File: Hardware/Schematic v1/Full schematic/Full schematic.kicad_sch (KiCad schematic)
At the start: 324 parts, among them J1 Conn_01x02_Male, J10 Conn_01x01_Male, J2 Reset, J3 Encoder, J4 Failure LED, J5 Bluetooth, J6 Conn_01x02_Male, J7 Display, J8 Buttons, J9 Conn_01x02_Male, K1 EDR101A0500, K2 EDR101A0500, K3 EDR101A0500, K4 EDR101A0500, K5 EDR101A0500, K6 EDR101A0500, Q1 BC847, Q10 IRLML6402, Q11 BC847, Q12 IRFZ44, Q13 BC847, Q14 BSS138, Q15 BC847, Q16 IRF610, Q17 BC847, Q18 IRLML6402, Q19 BC847, Q2 BC847, Q20 BFS17, Q21 IRLML6402, Q22 AFT05MS003N, Q23 IRLML2502, Q24 IRLML2502, Q25 IRLML2502, Q26 IRLML2502, Q27 IRLML2502, Q28 IRLML2502, Q3 BC847, Q4 BC847, Q5 BC847, Q6 IRLML6402, Q7 IRF4905, Q8 IRLML6402, Q9 IRLML6402, U1 74LVC2T45DC, U10 ICS501, U11 STM32F103C8Tx, U12 CAT24C256, U2 74LVC2T45DC, U3 AD9835, U4 LM27313XMF, U5 LM2734X, U6 LM2734X, U7 MAX1837EUT33-T, U8 UC3843_SOIC8, U9 AD5245BRJZ10, X1 50MHz, Y1 8MHz, Y2 32768Hz

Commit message: MCU is able to shut-down most of 3.3V-powered circuits to reduce battery consumption
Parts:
- added Q?: BC847, Package_TO_SOT_SMD:SOT-23, symbol Transistor_BJT:BC847
- added Q?: IRLML6402, Package_TO_SOT_SMD:SOT-23, symbol Transistor_FET:IRLML6402
- added R? (x2): 10k, Resistor_SMD:R_0805_2012Metric_Pad1.20x1.40mm_HandSolder, symbol Device:R
- added R?: 10, Resistor_SMD:R_0805_2012Metric_Pad1.20x1.40mm_HandSolder, symbol Device:R
- added R?: 47k, Resistor_SMD:R_0805_2012Metric_Pad1.20x1.40mm_HandSolder, symbol Device:R
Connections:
- net GND: now also Q?.2 (E), R?.2
- net REG_3.3V: now also Q?.2 (S), R?.1; no longer C106.2, C2.1, C3.1, C62.1, R76.1, R78.1, R82.1, R84.1, R85.1, R86.1, R88.1, R89.1, R90.1, U1.1 (VCCA), U1.5 (DIR), U12.8 (VCC), U2.1 (VCCA), U2.5 (DIR), U9.2 (Vdd)
- net ACTIVATE_3.3V: now reaches U11.28 (PB15)
- net ACTIVATE_3.3V: now also R?.1, R?.2
- new net: Q?.1 (B), R?.1
- new net: Q?.3 (C), R?.2
- new net: Q?.1 (G), R?.1, R?.2
- new net SW_3.3V: C106.2, C2.1, C3.1, C62.1, Q?.3 (D), R76.1, R78.1, R82.1, R84.1, R85.1, R86.1, R88.1, R89.1, R90.1, U1.1 (VCCA), U1.5 (DIR), U12.8 (VCC), U2.1 (VCCA), U2.5 (DIR), U9.2 (Vdd)
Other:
- note added: "Switcheable 3.3V"
- moved on the sheet: R11, R17, R4, R5

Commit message: Removed 30 capacitors from antenna tuner by swithcing to high-voltage capacitors
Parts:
- removed C100, C101, C102, C103, C104: 200pF, Capacitor_SMD:C_0805_2012Metric_Pad1.18x1.45mm_HandSolder, symbol Device:C
- removed C112, C113, C114, C115, C116: 100pF, Capacitor_SMD:C_0805_2012Metric_Pad1.18x1.45mm_HandSolder, symbol Device:C
- removed C118, C119, C120, C121, C122: 47pF, Capacitor_SMD:C_0805_2012Metric_Pad1.18x1.45mm_HandSolder, symbol Device:C
- removed C124, C125, C126, C127, C128: 24pF, Capacitor_SMD:C_0805_2012Metric_Pad1.18x1.45mm_HandSolder, symbol Device:C
- removed C130, C131, C132, C133, C134: 12pF, Capacitor_SMD:C_0805_2012Metric_Pad1.18x1.45mm_HandSolder, symbol Device:C
- removed C85, C86, C87, C88, C89: 390pF, Capacitor_SMD:C_0805_2012Metric_Pad1.18x1.45mm_HandSolder, symbol Device:C
- added C?: 2pF 250V, Capacitor_SMD:C_0805_2012Metric_Pad1.18x1.45mm_HandSolder, symbol Device:C
- C105: value 200pF -> 32pF 250V
- C117: value 100pF -> 16pF 250V
- C123: value 47pF -> 8pF 250V
- C129: value 24pF -> 4pF 250V
- C135: value 12pF -> 2pF 250V
- C90: value 390pF -> 62pF 250V
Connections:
- net ANT_3.5: now also C105.1, C117.1, C123.1, C129.1, C135.1, C90.1, C?.1
- net at C90.2, K1.1: now also C?.2
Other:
- note removed: "16pF"
- note removed: "2pF"
- note removed: "32pF"
- note removed: "4pF"
- note removed: "64pF"
- note removed: "8pF"
- moved on the sheet: C1, C10, C105, C106, C107, C108, C109, C11, C110, C111, C117, C12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

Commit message: New antenna matcher with smaller relays
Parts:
- removed C105: 32pF 250V, Capacitor_SMD:C_0805_2012Metric_Pad1.18x1.45mm_HandSolder, symbol Device:C
- removed C117: 16pF 250V, Capacitor_SMD:C_0805_2012Metric_Pad1.18x1.45mm_HandSolder, symbol Device:C
- removed C123: 8pF 250V, Capacitor_SMD:C_0805_2012Metric_Pad1.18x1.45mm_HandSolder, symbol Device:C
- removed C129: 4pF 250V, Capacitor_SMD:C_0805_2012Metric_Pad1.18x1.45mm_HandSolder, symbol Device:C
- removed K1, K2, K3, K4, K5, K6: EDR101A0500, Relay_THT:Relay_SPST_StandexMeder_SIL_Form1A, symbol Full-schematic-rescue:EDR101A0500-Fossa_library
- removed Q23, Q24: IRLML2502, Package_TO_SOT_SMD:SOT-23, symbol Device:Q_NMOS_GSD
- removed R87, R92, R93, R94: 100, Resistor_SMD:R_0805_2012Metric_Pad1.20x1.40mm_HandSolder, symbol Device:R
- added C101: 16pF 250V, Capacitor_SMD:C_0805_2012Metric_Pad1.18x1.45mm_HandSolder, symbol Device:C
- added C102: 8pF 250V, Capacitor_SMD:C_0805_2012Metric_Pad1.18x1.45mm_HandSolder, symbol Device:C
- added C103: 4pF 250V, Capacitor_SMD:C_0805_2012Metric_Pad1.18x1.45mm_HandSolder, symbol Device:C
- added C94: 32pF 250V, Capacitor_SMD:C_0805_2012Metric_Pad1.18x1.45mm_HandSolder, symbol Device:C
- added K1, K2, K3, K4, K5, K6: G6L-1F-DC5, G6L-1F-DC5, symbol G6L-1F-DC5:G6L-1F-DC5
- added Q28, Q29: IRLML2502, Package_TO_SOT_SMD:SOT-23, symbol Device:Q_NMOS_GSD
- added R95, R96, R97, R98: 100, Resistor_SMD:R_0805_2012Metric_Pad1.20x1.40mm_HandSolder, symbol Device:R
- gave numbers to parts that had none: 7
- renumbered C111 to C100, C135 to C104, C110 to C105, C109 to C106, C24 to C23, C23 to C24, C30 to C29, C29 to C30, C43 to C41, C41 to C42, C42 to C43, C57 to C56, C56 to C57, C69 to C68, C68 to C69, C84 to C85, C90 to C86, C91 to C87, C92 to C88, C93 to C89, C94 to C90, C95 to C91, C96 to C92, C97 to C93, C99 to C95, C98 to C96, C106 to C97, C108 to C98, C107 to C99, Q13 to Q15, Q14 to Q16, Q15 to Q17, Q16 to Q18, Q17 to Q19, Q18 to Q20, Q19 to Q21, Q21 to Q22, Q20 to Q23, Q22 to Q24, Q28 to Q30, R23 to R24, R24 to R25, R25 to R26, R26 to R27, R27 to R28, R28 to R29, R31 to R30, R29 to R31, R30 to R32, R32 to R34, R34 to R35, R35 to R36, R36 to R37, R37 to R38, R38 to R39, R39 to R40, R40 to R41, R41 to R42, R42 to R43, R43 to R44, R44 to R45, R45 to R46, R46 to R47, R47 to R48, R48 to R52, R49 to R53, R50 to R54, R51 to R55, R52 to R56, R53 to R57, R54 to R58, R55 to R59, R56 to R60, R57 to R61, R58 to R62, R59 to R63, R60 to R64, R61 to R65, R62 to R66, R63 to R67, R64 to R68, R65 to R69, R66 to R70, R68 to R71, R67 to R72, R69 to R73, R70 to R74, R71 to R75, R72 to R76, R73 to R77, R74 to R78, R75 to R79, R76 to R80, R77 to R81, R79 to R82, R78 to R83, R80 to R84, R81 to R85, R82 to R86, R83 to R87, R84 to R88, R85 to R89, R86 to R90, R88 to R92, R89 to R93, R90 to R94, R95 to R99
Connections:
- net ANT_3.5: now also C101.1, C102.1, C103.1, C94.1
- net GND: now also K1.2 (4), K2.2 (4), K3.2 (4), K4.2 (4), K5.2 (4), K6.2 (4), Q28.2 (S), Q29.2 (S)
- net MATCH_1: now also R98.2
- net MATCH_2: now also R97.2
- net MATCH_3: now also R96.2
- net MATCH_4: now also R95.2; no longer R91.2
- net MATCH_5: now also R91.2
- net PWR_3.5_5: now also K1.4 (8), K2.4 (8), K3.4 (8), K4.4 (8), K5.4 (8), K6.4 (8)
- net at C84.2, C86.2: now also K1.1 (2)
- net at Q25.3 (D): now also K1.3 (5)
- net at Q26.3 (D): now also K2.3 (5)
- net at Q27.3 (D): now also K3.3 (5)
- net at R91.1: now also Q25.1 (G)
- net at Q26.1 (G): now also R95.1
- net at Q27.1 (G): now also R96.1
- net at C104.2: now also K6.1 (2)
- net at Q30.3 (D): now also K6.3 (5)
- new net: Q29.1 (G), R98.1
- new net: K5.3 (5), Q29.3 (D)
- new net: C94.2, K2.1 (2)
- new net: C103.2, K5.1 (2)
- new net: C102.2, K4.1 (2)
- new net: K4.3 (5), Q28.3 (D)
- new net: C101.2, K3.1 (2)
- new net: Q28.1 (G), R97.1
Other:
- moved on the sheet: C104, C105, C106, C84, C86, Q30, R99

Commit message: Prepared to start PCB tracing
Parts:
- K1, K2, K3, K4, K5, K6: footprint G6L-1F-DC5 -> SamacSys:G6L-1F-DC5
- U7: footprint (none) -> Package_TO_SOT_SMD:TSOT-23-6
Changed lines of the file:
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@@
     (property "Reference" "U7" (id 0) (at 165.1 392.591 0))
     (property "Value" "MAX1837EUT33-T" (id 1) (at 165.1 395.1279 0))
-    (property "Footprint" " " (id 2) (at 165.1 394.97 0)
+    (property "Footprint" "Package_TO_SOT_SMD:TSOT-23-6" (id 2) (at 165.1 394.97 0)
       (effects (font (size 1.27 1.27)) hide)
     )
@@
     (property "Reference" "K2" (id 0) (at 459.105 38.261 0))
     (property "Value" "G6L-1F-DC5" (id 1) (at 459.105 40.7979 0))
-    (property "Footprint" "G6L-1F-DC5" (id 2) (at 465.455 41.91 0)
+    (property "Footprint" "SamacSys:G6L-1F-DC5" (id 2) (at 465.455 41.91 0)
       (effects (font (size 1.27 1.27)) (justify left) hide)
     )
@@
     (property "Reference" "K5" (id 0) (at 541.02 38.261 0))
     (property "Value" "G6L-1F-DC5" (id 1) (at 541.02 40.7979 0))
-    (property "Footprint" "G6L-1F-DC5" (id 2) (at 547.37 41.91 0)
+    (property "Footprint" "SamacSys:G6L-1F-DC5" (id 2) (at 547.37 41.91 0)
       (effects (font (size 1.27 1.27)) (justify left) hide)
     )
@@
     (property "Reference" "K4" (id 0) (at 513.715 38.261 0))
     (property "Value" "G6L-1F-DC5" (id 1) (at 513.715 40.7979 0))
-    (property "Footprint" "G6L-1F-DC5" (id 2) (at 520.065 41.91 0)
+    (property "Footprint" "SamacSys:G6L-1F-DC5" (id 2) (at 520.065 41.91 0)
       (effects (font (size 1.27 1.27)) (justify left) hide)
     )
@@
     (property "Reference" "K1" (id 0) (at 431.8 38.261 0))
     (property "Value" "G6L-1F-DC5" (id 1) (at 431.8 40.7979 0))
-    (property "Footprint" "G6L-1F-DC5" (id 2) (at 438.15 41.91 0)
+    (property "Footprint" "SamacSys:G6L-1F-DC5" (id 2) (at 438.15 41.91 0)
       (effects (font (size 1.27 1.27)) (justify left) hide)
     )
@@
     (property "Reference" "K6" (id 0) (at 568.325 38.261 0))
     (property "Value" "G6L-1F-DC5" (id 1) (at 568.325 40.7979 0))
-    (property "Footprint" "G6L-1F-DC5" (id 2) (at 574.675 41.91 0)
+    (property "Footprint" "SamacSys:G6L-1F-DC5" (id 2) (at 574.675 41.91 0)
       (effects (font (size 1.27 1.27)) (justify left) hide)
     )
@@
     (property "Reference" "K3" (id 0) (at 486.41 38.261 0))
     (property "Value" "G6L-1F-DC5" (id 1) (at 486.41 40.7979 0))
-    (property "Footprint" "G6L-1F-DC5" (id 2) (at 492.76 41.91 0)
+    (property "Footprint" "SamacSys:G6L-1F-DC5" (id 2) (at 492.76 41.91 0)
       (effects (font (size 1.27 1.27)) (justify left) hide)
     )
@@
     )
     (path "/a2e1440b-e257-4d0a-808d-5710ecf6f920"
-      (reference "K1") (unit 1) (value "G6L-1F-DC5") (footprint "G6L-1F-DC5")
+      (reference "K1") (unit 1) (value "G6L-1F-DC5") (footprint "SamacSys:G6L-1F-DC5")
     )
     (path "/324106b3-abb2-420f-a627-0aac5e60675f"
-      (reference "K2") (unit 1) (value "G6L-1F-DC5") (footprint "G6L-1F-DC5")
+      (reference "K2") (unit 1) (value "G6L-1F-DC5") (footprint "SamacSys:G6L-1F-DC5")
     )
     (path "/d89a0302-120b-4752-9963-58f61b530fff"
-      (reference "K3") (unit 1) (value "G6L-1F-DC5") (footprint "G6L-1F-DC5")
+      (reference "K3") (unit 1) (value "G6L-1F-DC5") (footprint "SamacSys:G6L-1F-DC5")
     )
     (path "/4aa9f57c-e3bb-4992-9327-b49e49f538a5"
-      (reference "K4") (unit 1) (value "G6L-1F-DC5") (footprint "G6L-1F-DC5")
+      (reference "K4") (unit 1) (value "G6L-1F-DC5") (footprint "SamacSys:G6L-1F-DC5")
     )
     (path "/423851f6-93ed-4dfc-9519-566e79596147"
-      (reference "K5") (unit 1) (value "G6L-1F-DC5") (footprint "G6L-1F-DC5")
+      (reference "K5") (unit 1) (value "G6L-1F-DC5") (footprint "SamacSys:G6L-1F-DC5")
     )
     (path "/bc52d2ea-23a3-403b-8c59-ec7d15d1e2a6"
-      (reference "K6") (unit 1) (value "G6L-1F-DC5") (footprint "G6L-1F-DC5")
+      (reference "K6") (unit 1) (value "G6L-1F-DC5") (footprint "SamacSys:G6L-1F-DC5")
     )
     (path "/00000000-0000-0000-0000-000060d7cf1a"
@@
     )
     (path "/2d6c91ba-d03a-44df-a397-8d992093a3d4"
-      (reference "U7") (unit 1) (value "MAX1837EUT33-T") (footprint " ")
+      (reference "U7") (unit 1) (value "MAX1837EUT33-T") (footprint "Package_TO_SOT_SMD:TSOT-23-6")
     )
     (path "/00000000-0000-0000-0000-000060b1e62b"

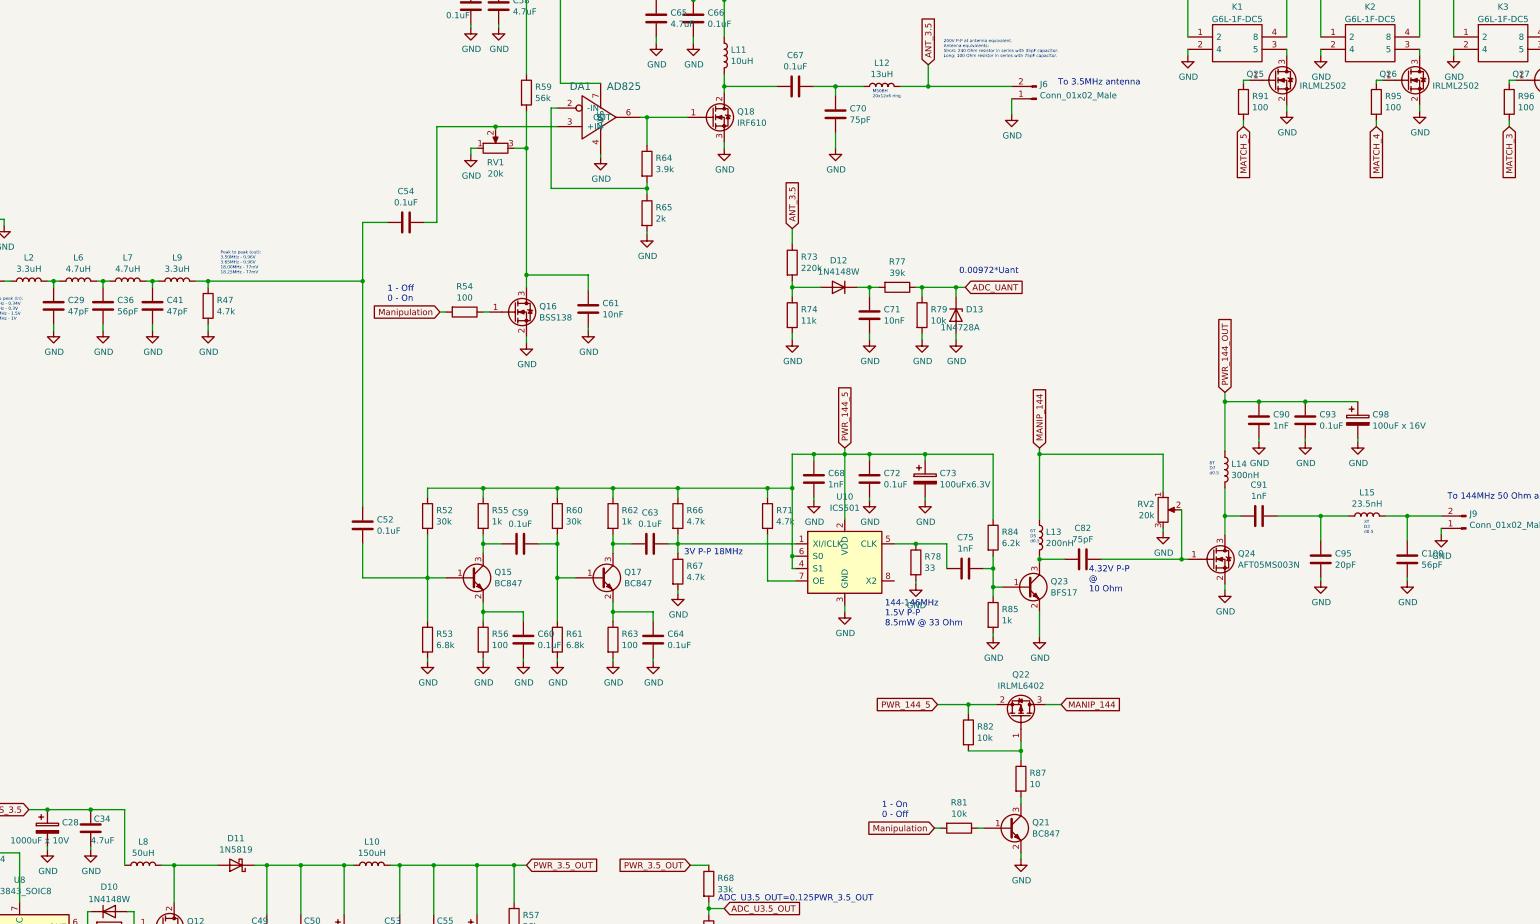
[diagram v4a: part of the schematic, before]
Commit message: All inductors are SMD now
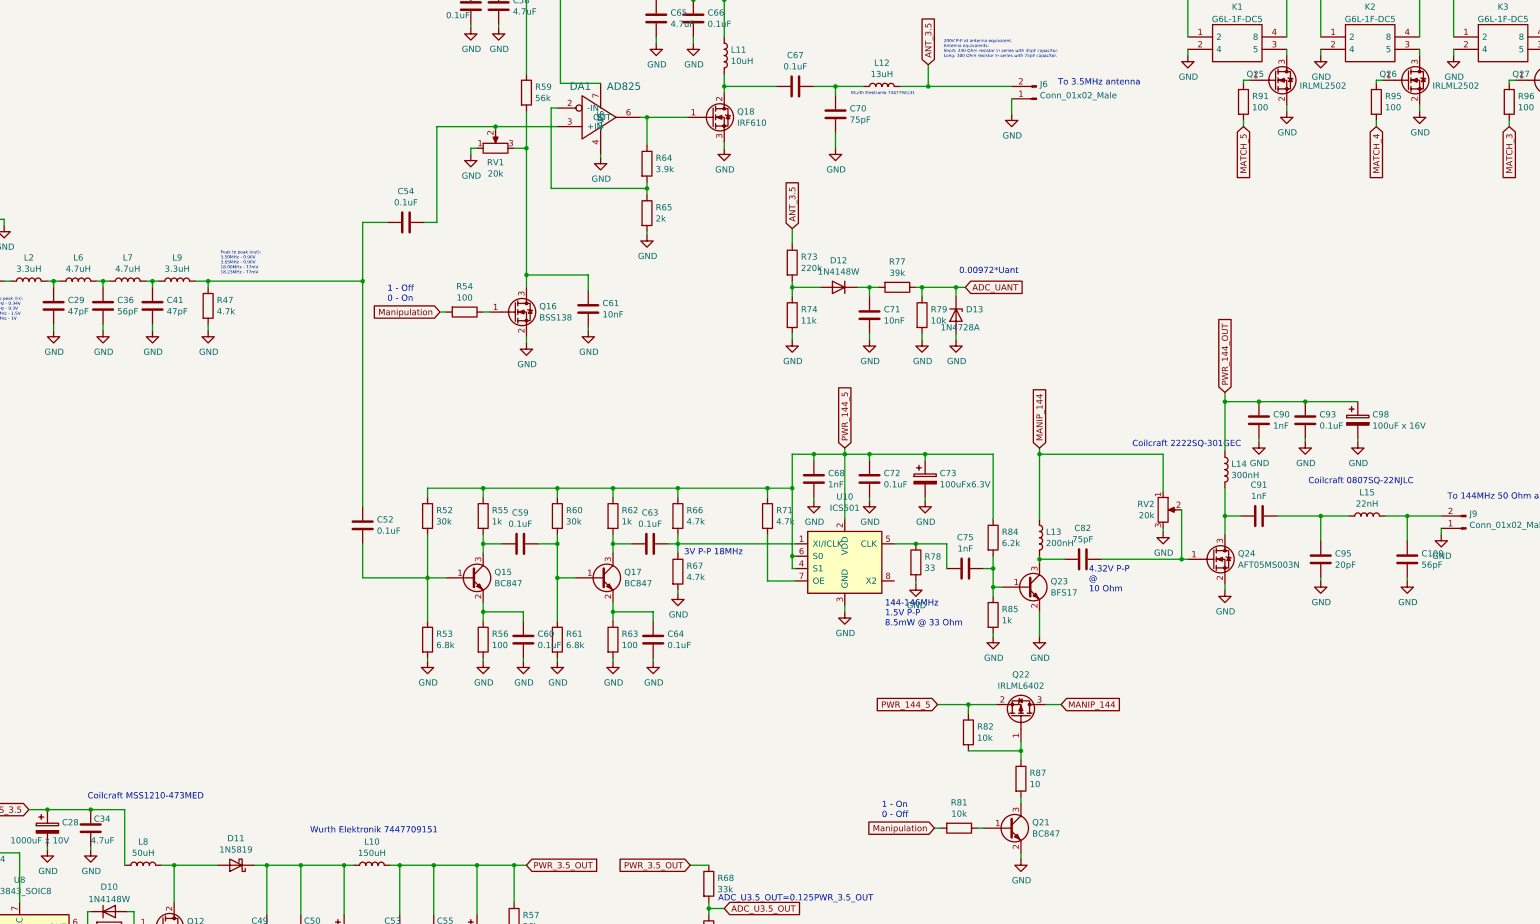
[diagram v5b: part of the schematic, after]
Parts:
- C1: footprint Capacitor_THT:CP_Radial_D6.3mm_P2.50mm -> Inductor_SMD:L_0603_1608Metric_Pad1.05x0.95mm_HandSolder
- L12: footprint Inductor_THT:L_Toroid_Vertical_L21.6mm_W9.1mm_P8.40mm_Bourns_5700 -> Inductor_SMD:L_10.4x10.4_H4.8
- L13: footprint Inductor_THT:L_Axial_L5.3mm_D2.2mm_P7.62mm_Horizontal_Vishay_IM-1 -> Inductor_SMD:L_0603_1608Metric_Pad1.05x0.95mm_HandSolder
- L14: footprint Inductor_THT:L_Axial_L16.0mm_D7.5mm_P7.62mm_Vertical_Fastron_XHBCC -> Inductor_SMD:L_Pulse_PA4320
- L15: value 23.5nH -> 22nH; footprint Inductor_THT:L_Axial_L9.5mm_D4.0mm_P5.08mm_Vertical_Fastron_SMCC -> Inductor_SMD:L_1206_3216Metric_Pad1.22x1.90mm_HandSolder
- L8: footprint Inductor_THT:L_Toroid_Vertical_L25.4mm_W14.7mm_P12.20mm_Vishay_TJ5_BigPads -> Inductor_SMD:L_12x12mm_H8mm
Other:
- note added: "Coilcraft 0807SQ-22NJLC"
- note added: "Coilcraft 2222SQ-301GEC"
- note added: "Coilcraft MSS1210-473MED"
- note added: "Wurth Elektronik 7447709151"
- note added: "Wurth Elektronik 7447798131"
- note removed: "3T D3 d0.5"
- note removed: "6T D5 d0.5"
- note removed: "8T D7 d0.5"
- note removed: "M50BH 20x12x6 ring"
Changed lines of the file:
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@@
     (effects (font (size 1.27 1.27)) (justify left bottom))
   )
-  (text "ADC_U3.5_OUT=0.125PWR_3.5_OUT" (at 325.12 222.25 0)
+  (text "Coilcraft 0807SQ-22NJLC" (at 446.405 136.525 0)
     (effects (font (size 1.27 1.27)) (justify left bottom))
   )
-  (text "6T\nD5\nd0.5" (at 389.255 148.59 0)
-    (effects (font (size 0.635 0.635)) (justify left bottom))
+  (text "ADC_U3.5_OUT=0.125PWR_3.5_OUT" (at 325.12 222.25 0)
+    (effects (font (size 1.27 1.27)) (justify left bottom))
   )
   (text "3V P-P 18MHz" (at 318.135 151.13 0)
@@
     (effects (font (size 1.27 1.27)) (justify left bottom))
   )
-  (text "GND" (at 375.285 391.16 0)
+  (text "Coilcraft MSS1210-473MED" (at 195.58 201.295 0)
     (effects (font (size 1.27 1.27)) (justify left bottom))
   )
-  (text "8T\nD7\nd0.5" (at 426.085 134.62 0)
-    (effects (font (size 0.635 0.635)) (justify left bottom))
+  (text "GND" (at 375.285 391.16 0)
+    (effects (font (size 1.27 1.27)) (justify left bottom))
   )
   (text "GND" (at 412.75 430.53 0)
     (effects (font (size 1.27 1.27)) (justify left bottom))
   )
-  (text "3T\nD3\nd0.5" (at 457.835 146.685 0)
-    (effects (font (size 0.635 0.635)) (justify left bottom))
-  )
   (text "Right" (at 411.48 427.99 0)
     (effects (font (size 1.27 1.27)) (justify left bottom))
@@
     (effects (font (size 1.27 1.27)) (justify left bottom))
   )
+  (text "Wurth Elektronik 7447709151" (at 241.3 208.28 0)
+    (effects (font (size 1.27 1.27)) (justify left bottom))
+  )
   (text "HC-06\nBluetooth" (at 365.76 392.43 0)
     (effects (font (size 1.27 1.27)) (justify left bottom))
@@
     (effects (font (size 1.27 1.27)) (justify left bottom))
   )
+  (text "Coilcraft 2222SQ-301GEC" (at 410.21 128.905 0)
+    (effects (font (size 1.27 1.27)) (justify left bottom))
+  )
   (text "VCC" (at 407.67 390.525 0)
     (effects (font (size 1.27 1.27)) (justify left bottom))
@@
     (effects (font (size 1.27 1.27)) (justify left bottom))
   )
-  (text "M50BH\n20x12x6 ring" (at 356.87 57.15 0)
+  (text "Wurth Elektronik 7447798131" (at 352.425 56.515 0)
     (effects (font (size 0.635 0.635)) (justify left bottom))
   )
@@
     (property "Reference" "L12" (id 0) (at 358.775 49.784 90))
     (property "Value" "13uH" (id 1) (at 358.775 52.0954 90))
-    (property "Footprint" "Inductor_THT:L_Toroid_Vertical_L21.6mm_W9.1mm_P8.40mm_Bourns_5700" (id 2) (at 358.775 54.61 0)
+    (property "Footprint" "Inductor_SMD:L_10.4x10.4_H4.8" (id 2) (at 358.775 54.61 0)
       (effects (font (size 1.27 1.27)) hide)
     )
@@
       (effects (font (size 1.27 1.27)) (justify left))
     )
-    (property "Footprint" "Inductor_THT:L_Axial_L5.3mm_D2.2mm_P7.62mm_Horizontal_Vishay_IM-1" (id 2) (at 391.16 147.32 0)
+    (property "Footprint" "Inductor_SMD:L_0603_1608Metric_Pad1.05x0.95mm_HandSolder" (id 2) (at 391.16 147.32 0)
       (effects (font (size 1.27 1.27)) hide)
     )
@@
       (effects (font (size 1.27 1.27)) (justify left))
     )
-    (property "Footprint" "Inductor_THT:L_Axial_L16.0mm_D7.5mm_P7.62mm_Vertical_Fastron_XHBCC" (id 2) (at 429.26 133.35 0)
+    (property "Footprint" "Inductor_SMD:L_Pulse_PA4320" (id 2) (at 429.26 133.35 0)
       (effects (font (size 1.27 1.27)) hide)
     )
@@
     (in_bom yes) (on_board yes)
     (property "Reference" "L15" (id 0) (at 458.47 138.049 90))
-    (property "Value" "23.5nH" (id 1) (at 458.47 140.3604 90))
-    (property "Footprint" "Inductor_THT:L_Axial_L9.5mm_D4.0mm_P5.08mm_Vertical_Fastron_SMCC" (id 2) (at 458.47 142.875 0)
+    (property "Value" "22nH" (id 1) (at 458.47 140.3604 90))
+    (property "Footprint" "Inductor_SMD:L_1206_3216Metric_Pad1.22x1.90mm_HandSolder" (id 2) (at 458.47 142.875 0)
       (effects (font (size 1.27 1.27)) hide)
     )
@@
     (property "Reference" "L8" (id 0) (at 207.01 209.804 90))
     (property "Value" "50uH" (id 1) (at 207.01 212.1154 90))
-    (property "Footprint" "Inductor_THT:L_Toroid_Vertical_L25.4mm_W14.7mm_P12.20mm_Vishay_TJ5_BigPads" (id 2) (at 207.01 214.63 0)
+    (property "Footprint" "Inductor_SMD:L_12x12mm_H8mm" (id 2) (at 207.01 214.63 0)
       (effects (font (size 1.27 1.27)) hide)
     )
@@
       (effects (font (size 1.27 1.27)) (justify left))
     )
-    (property "Footprint" "Capacitor_THT:CP_Radial_D6.3mm_P2.50mm" (id 2) (at 40.9702 231.14 0)
+    (property "Footprint" "Inductor_SMD:L_0603_1608Metric_Pad1.05x0.95mm_HandSolder" (id 2) (at 40.9702 231.14 0)
       (effects (font (size 1.27 1.27)) hide)
     )
@@
     )
     (path "/00000000-0000-0000-0000-000060da81bd"
-      (reference "C1") (unit 1) (value "100uFx16V") (footprint "Capacitor_THT:CP_Radial_D6.3mm_P2.50mm")
+      (reference "C1") (unit 1) (value "100uFx16V") (footprint "Inductor_SMD:L_0603_1608Metric_Pad1.05x0.95mm_HandSolder")
     )
     (path "/00000000-0000-0000-0000-00005fded36d"
@@
     )
     (path "/00000000-0000-0000-0000-000060b1f685"
-      (reference "L8") (unit 1) (value "50uH") (footprint "Inductor_THT:L_Toroid_Vertical_L25.4mm_W14.7mm_P12.20mm_Vishay_TJ5_BigPads")
+      (reference "L8") (unit 1) (value "50uH") (footprint "Inductor_SMD:L_12x12mm_H8mm")
     )
     (path "/00000000-0000-0000-0000-00005fe38cf5"
@@
     )
     (path "/00000000-0000-0000-0000-00005fe874d4"
-      (reference "L12") (unit 1) (value "13uH") (footprint "Inductor_THT:L_Toroid_Vertical_L21.6mm_W9.1mm_P8.40mm_Bourns_5700")
+      (reference "L12") (unit 1) (value "13uH") (footprint "Inductor_SMD:L_10.4x10.4_H4.8")
     )
     (path "/00000000-0000-0000-0000-0000602f0f19"
-      (reference "L13") (unit 1) (value "200nH") (footprint "Inductor_THT:L_Axial_L5.3mm_D2.2mm_P7.62mm_Horizontal_Vishay_IM-1")
+      (reference "L13") (unit 1) (value "200nH") (footprint "Inductor_SMD:L_0603_1608Metric_Pad1.05x0.95mm_HandSolder")
     )
     (path "/00000000-0000-0000-0000-0000603f4aa9"
-      (reference "L14") (unit 1) (value "300nH") (footprint "Inductor_THT:L_Axial_L16.0mm_D7.5mm_P7.62mm_Vertical_Fastron_XHBCC")
+      (reference "L14") (unit 1) (value "300nH") (footprint "Inductor_SMD:L_Pulse_PA4320")
     )
     (path "/00000000-0000-0000-0000-00006054d4c1"
-      (reference "L15") (unit 1) (value "23.5nH") (footprint "Inductor_THT:L_Axial_L9.5mm_D4.0mm_P5.08mm_Vertical_Fastron_SMCC")
+      (reference "L15") (unit 1) (value "22nH") (footprint "Inductor_SMD:L_1206_3216Metric_Pad1.22x1.90mm_HandSolder")
     )
     (path "/00000000-0000-0000-0000-0000629d426f"
